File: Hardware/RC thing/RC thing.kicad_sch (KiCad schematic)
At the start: 2 parts, among them J1 Li_bat, U101 NRF24L01_Breakout

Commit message: RC thing schematic 70% done
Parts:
- removed J1: Li_bat, symbol Connector_Generic:Conn_01x02
- added H1, H2, H3, H4: MountingHole, MountingHole:MountingHole_2.7mm_M2.5, symbol Mechanical:MountingHole
- added J1: Conn_01x04, symbol Connector_Generic:Conn_01x04
- added RV1, RV2: 4.7k, symbol Device:R_Potentiometer
- added SW2, SW3: SW_Push, symbol Switch:SW_Push
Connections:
- net +3.3V: now also J1.2 (Pin_2)
- net GND: now also J1.1 (Pin_1), RV1.3, RV2.3, SW2.1, SW3.1
- net IRQ: now reaches U101.8 (IRQ)
- net CSN renamed GPIO8
- new net +3V3: RV1.1, RV2.1
- new net GPIO12: J1.4 (Pin_4)
- new net GPIO13: J1.3 (Pin_3)
- new net GPIO26: RV1.2
- new net GPIO27: RV2.2
- new net GPIO4: SW2.2
- new net GPIO5: SW3.2
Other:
- added sheet BMS (bms.kicad_sch)
- note added: "Analog sticks"
- note added: "Buttons (not sure how many we'll need)"
- note added: "OLED"
- title: (none) -> SPRO3D RC remote PCB
- moved on the sheet: U101

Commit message: 90%
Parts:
- added SW4: SW_Push, symbol Switch:SW_Push
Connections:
- net GND: now also SW4.1
- net GPIO4: now also SW3.2; no longer SW2.2
- net GPIO5: now also SW4.2; no longer SW3.2
- new net GPIO3: SW2.2
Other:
- moved on the sheet: J1, RV1, RV2, SW2, SW3

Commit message: more rc stuff (trust)
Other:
- sheet BMS renamed BMS and power
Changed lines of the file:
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@@
 	(wire
 		(pts
-			(xy 50.8 67.31) (xy 50.8 80.01)
+			(xy 50.8 68.58) (xy 50.8 80.01)
+		)
+		(stroke
+			(width 0)
+			(type default)
+		)
+	)
+	(wire
+		(pts
+			(xy 54.61 66.04) (xy 54.61 82.55)
 		)
 		(stroke
@@
 	(wire
 		(pts
-			(xy 46.99 67.31) (xy 50.8 67.31)
+			(xy 46.99 68.58) (xy 50.8 68.58)
 		)
 		(stroke
@@
 	(wire
 		(pts
+			(xy 46.99 66.04) (xy 54.61 66.04)
+		)
+		(stroke
+			(width 0)
+			(type default)
+		)
+	)
+	(wire
+		(pts
 			(xy 46.99 35.56) (xy 57.15 35.56)
 		)
@@
 		(pts
 			(xy 130.81 39.37) (xy 130.81 45.72)
+		)
+		(stroke
+			(width 0)
+			(type default)
+		)
+	)
+	(wire
+		(pts
+			(xy 54.61 82.55) (xy 46.99 82.55)
 		)
 		(stroke
@@
 	(hierarchical_label "GPIO11"
 		(shape tri_state)
-		(at 46.99 67.31 180)
+		(at 46.99 68.58 180)
 		(effects
 			(font
@@
 		)
 	)
-	(hierarchical_label "Batt_status"
+	(hierarchical_label "Charge_status"
 		(shape output)
 		(at 46.99 80.01 180)
@@
 		)
 	)
+	(hierarchical_label "Battery_voltage_level"
+		(shape output)
+		(at 46.99 82.55 180)
+		(effects
+			(font
+				(size 1.27 1.27)
+			)
+			(justify right)
+		)
+	)
 	(hierarchical_label "GPIO4"
 		(shape tri_state)
 		(at 46.99 53.34 180)
+		(effects
+			(font
+				(size 1.27 1.27)
+			)
+			(justify right)
+		)
+	)
+	(hierarchical_label "GPIO28"
+		(shape tri_state)
+		(at 46.99 66.04 180)
 		(effects
 			(font
@@
 	)
 	(sheet
-		(at 25.4 78.105)
-		(size 21.59 12.7)
+		(at 23.495 78.105)
+		(size 23.495 12.7)
 		(exclude_from_sim no)
 		(in_bom yes)
@@
 			(color 0 0 0 0.0000)
 		)
-		(property "Sheetname" "BMS"
-			(at 25.4 77.3934 0)
+		(property "Sheetname" "BMS and power"
+			(at 23.495 77.3934 0)
 			(effects
 				(font
@@
 		)
 		(property "Sheetfile" "bms.kicad_sch"
-			(at 25.4 91.3896 0)
+			(at 23.495 91.3896 0)
 			(effects
 				(font
@@
 	)
 	(sheet
-		(at 25.4 24.13)
-		(size 21.59 46.99)
+		(at 23.495 24.13)
+		(size 23.495 46.99)
 		(exclude_from_sim no)
 		(in_bom yes)
@@
 		)
 		(property "Sheetname" "RP2040"
-			(at 25.4 23.4184 0)
+			(at 23.495 23.4184 0)
 			(effects
 				(font
@@
 		)
 		(property "Sheetfile" "rp2040.kicad_sch"
-			(at 25.4 71.7046 0)
-			(effects
-				(font
+			(at 23.495 71.7046 0)
+			(effects
+				(font

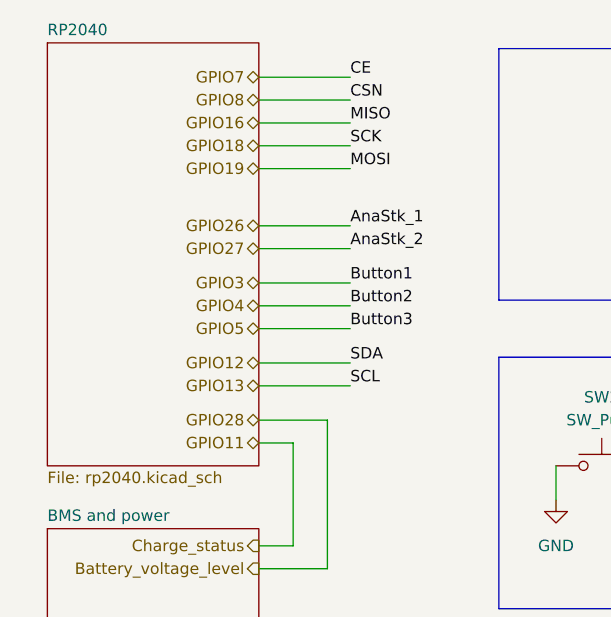
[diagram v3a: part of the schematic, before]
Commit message: update pin layout to make PCB easier
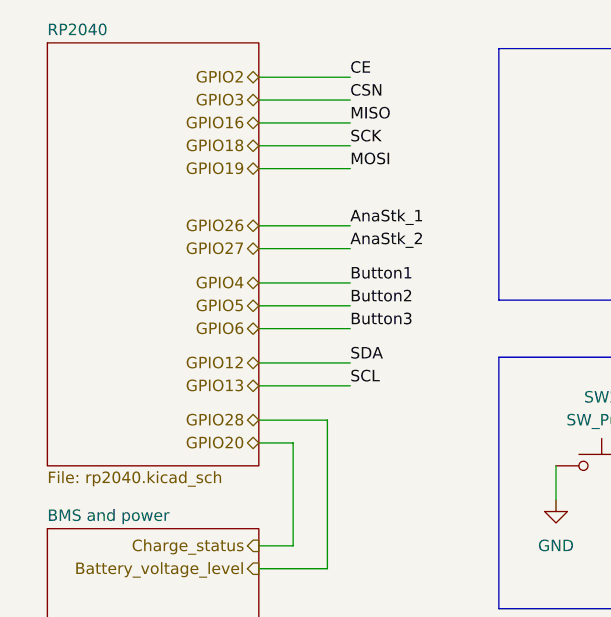
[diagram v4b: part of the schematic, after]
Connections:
- net GPIO8 is gone; now on net GPIO3: U101.4 (~{CSN})
- net GPIO3: no longer SW2.2
- net GPIO4: now also SW2.2; no longer SW3.2
- net GPIO5: now also SW3.2; no longer SW4.2
- net GPIO7 renamed GPIO2
- new net GPIO6: SW4.2
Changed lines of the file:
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@@
 		)
 	)
-	(hierarchical_label "GPIO7"
+	(hierarchical_label "GPIO2"
 		(shape tri_state)
 		(at 46.99 27.94 180)
@@
 		)
 	)
-	(hierarchical_label "GPIO5"
+	(hierarchical_label "GPIO6"
 		(shape tri_state)
 		(at 46.99 55.88 180)
@@
 		)
 	)
-	(hierarchical_label "GPIO11"
+	(hierarchical_label "GPIO20"
 		(shape tri_state)
 		(at 46.99 68.58 180)
@@
 		)
 	)
-	(hierarchical_label "GPIO8"
+	(hierarchical_label "GPIO3"
 		(shape tri_state)
 		(at 46.99 30.48 180)
@@
 		)
 	)
-	(hierarchical_label "GPIO3"
+	(hierarchical_label "GPIO4"
 		(shape tri_state)
 		(at 46.99 50.8 180)
@@
 		)
 	)
-	(hierarchical_label "GPIO4"
+	(hierarchical_label "GPIO5"
 		(shape tri_state)
 		(at 46.99 53.34 180)

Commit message: more pinout changes :upside_down_smile:
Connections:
- net GPIO12 renamed GPIO0
- net GPIO13 renamed GPIO1
- net GPIO2 renamed GPIO20
- net GPIO3 renamed GPIO21
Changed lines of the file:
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@@
 		)
 	)
-	(hierarchical_label "GPIO2"
+	(hierarchical_label "GPIO20"
 		(shape tri_state)
 		(at 46.99 27.94 180)
@@
 		)
 	)
-	(hierarchical_label "GPIO13"
+	(hierarchical_label "GPIO1"
 		(shape tri_state)
 		(at 46.99 62.23 180)
@@
 		)
 	)
-	(hierarchical_label "GPIO20"
+	(hierarchical_label "GPIO22"
 		(shape tri_state)
 		(at 46.99 68.58 180)
@@
 		)
 	)
-	(hierarchical_label "GPIO12"
+	(hierarchical_label "GPIO0"
 		(shape tri_state)
 		(at 46.99 59.69 180)
@@
 		)
 	)
-	(hierarchical_label "GPIO3"
+	(hierarchical_label "GPIO21"
 		(shape tri_state)
 		(at 46.99 30.48 180)

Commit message: RC thing PCB 95% trustworthy (six seven)
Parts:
- J1: footprint (none) -> Connector_PinHeader_2.54mm:PinHeader_1x04_P2.54mm_Vertical
- RV1, RV2: footprint (none) -> Connector_PinHeader_2.54mm:PinHeader_1x03_P2.54mm_Vertical
- SW2, SW3, SW4: footprint (none) -> Connector_PinHeader_2.54mm:PinHeader_1x02_P2.54mm_Vertical
- U101: footprint RF_Module:nRF24L01_Breakout -> Connector_PinHeader_2.54mm:PinHeader_2x04_P2.54mm_Vertical
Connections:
- net +3.3V is gone; now on net +3V3: J1.2 (Pin_2), U101.2 (VCC)
- net GPIO0 renamed SDA
- net GPIO1 renamed SCL
- net GPIO16 renamed MISO
- net GPIO18 renamed SCK
- net GPIO19 renamed MOSI
- net GPIO20 renamed CE
- net GPIO21 renamed CSN
- net GPIO26 renamed AnaStk_1
- net GPIO27 renamed AnaStk_2
- net GPIO4 renamed Button1
- net GPIO5 renamed Button2
- net GPIO6 renamed Button3
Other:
- sheet BMS and power ports: added Battery_voltage_level, Charge_status; removed none
- sheet RP2040 ports: added GPIO0, GPIO1, GPIO16, GPIO18, GPIO19, GPIO20, GPIO21, GPIO22, GPIO26_ADC0, GPIO27_ADC1, GPIO28_ADC2, GPIO4, GPIO5, GPIO6; removed none

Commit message: new RC PCB updates
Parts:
- RV1, RV2: footprint Connector_PinHeader_2.54mm:PinHeader_1x03_P2.54mm_Vertical -> Connector_JST:JST_PH_B3B-PH-K_1x03_P2.00mm_Vertical
- SW2, SW3, SW4: footprint Connector_PinHeader_2.54mm:PinHeader_1x02_P2.54mm_Vertical -> Connector_JST:JST_PH_B2B-PH-K_1x02_P2.00mm_Vertical
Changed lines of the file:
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@@
 			)
 		)
-		(property "Footprint" "Connector_PinHeader_2.54mm:PinHeader_1x02_P2.54mm_Vertical"
+		(property "Footprint" "Connector_JST:JST_PH_B2B-PH-K_1x02_P2.00mm_Vertical"
 			(at 85.09 66.04 0)
 			(effects
@@
 			)
 		)
-		(property "Footprint" "Connector_PinHeader_2.54mm:PinHeader_1x02_P2.54mm_Vertical"
+		(property "Footprint" "Connector_JST:JST_PH_B2B-PH-K_1x02_P2.00mm_Vertical"
 			(at 140.97 66.04 0)
 			(effects
@@
 			)
 		)
-		(property "Footprint" "Connector_PinHeader_2.54mm:PinHeader_1x03_P2.54mm_Vertical"
+		(property "Footprint" "Connector_JST:JST_PH_B3B-PH-K_1x03_P2.00mm_Vertical"
 			(at 93.98 39.37 0)
 			(effects
@@
 			)
 		)
-		(property "Footprint" "Connector_PinHeader_2.54mm:PinHeader_1x03_P2.54mm_Vertical"
+		(property "Footprint" "Connector_JST:JST_PH_B3B-PH-K_1x03_P2.00mm_Vertical"
 			(at 121.92 39.37 0)
 			(effects
@@
 			)
 		)
-		(property "Footprint" "Connector_PinHeader_2.54mm:PinHeader_1x02_P2.54mm_Vertical"
+		(property "Footprint" "Connector_JST:JST_PH_B2B-PH-K_1x02_P2.00mm_Vertical"
 			(at 113.03 66.04 0)
 			(effects

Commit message: trustworthy(?) RC PCB
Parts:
- J1: footprint Connector_PinHeader_2.54mm:PinHeader_1x04_P2.54mm_Vertical -> Connector_JST:JST_PH_B4B-PH-K_1x04_P2.00mm_Vertical
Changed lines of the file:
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@@
 			)
 		)
-		(property "Footprint" "Connector_PinHeader_2.54mm:PinHeader_1x04_P2.54mm_Vertical"
+		(property "Footprint" "Connector_JST:JST_PH_B4B-PH-K_1x04_P2.00mm_Vertical"
 			(at 167.64 35.56 0)
 			(effects
